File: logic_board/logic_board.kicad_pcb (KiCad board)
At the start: 4 copper layers, 80 x 30 mm, 55 parts, among them J1 Debug, J2 Audio In, J3 SJ2-3595X-SMT, J4 Amphenol 124015, J5 Batt, SW1 TL3315NF160Q, SW2 TL3315NF160Q, SW3 TL3315NF160Q, SW4 TL3315NF160Q, SW5 Power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

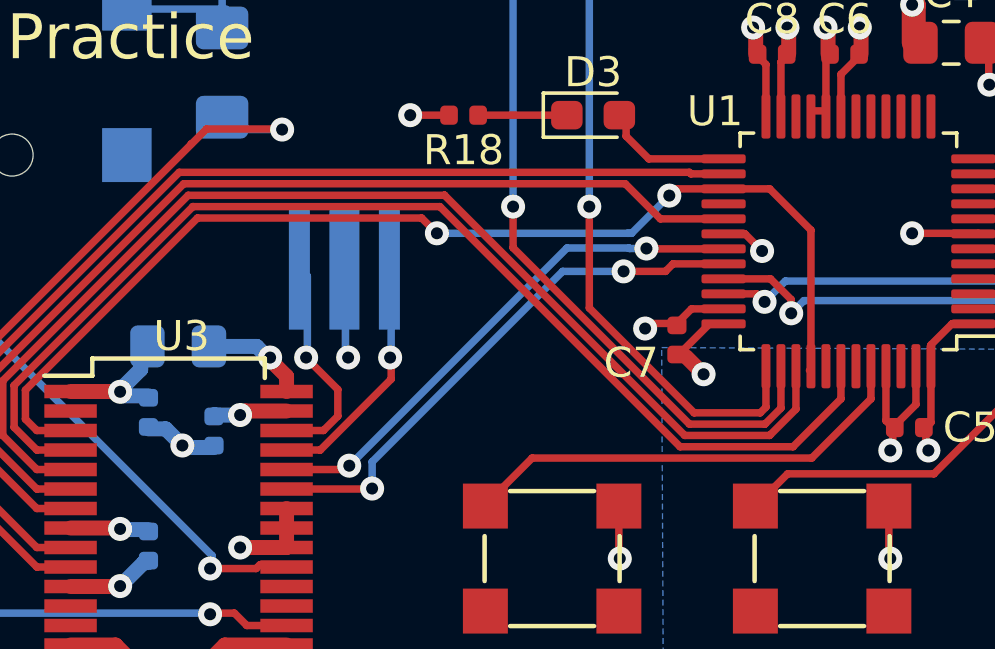
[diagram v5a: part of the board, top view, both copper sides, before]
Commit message: Fix I2C2_SDA, which was mislabeled in the STM32G473 datasheet.
It now connects to pin30. In the G474 datasheet, both places
that reference this pin agree.
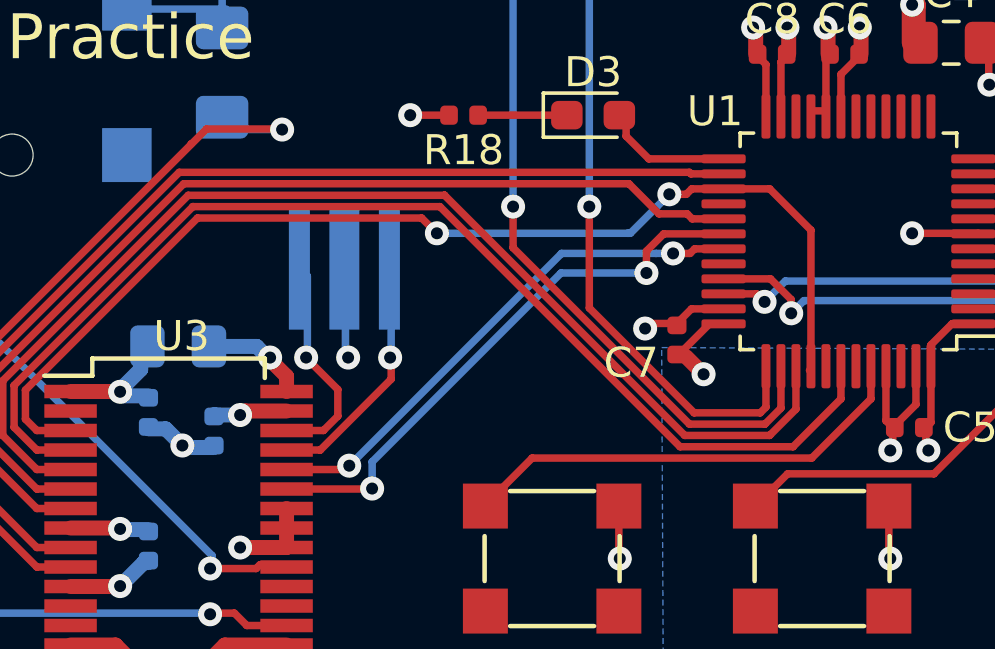
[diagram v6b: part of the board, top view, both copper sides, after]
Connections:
- U1 pad 30: Net-(U1-Pad30) -> SDA
- U1 pad 32: SDA -> Net-(U1-Pad32)
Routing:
- net Net-(U1-Pad30): track 1.77 -> 0.00 mm, vias 1 -> 0
- net SDA: track 18.0 -> 19.0 mm
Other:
- net class Default: trace_width 0.127 -> 0.25

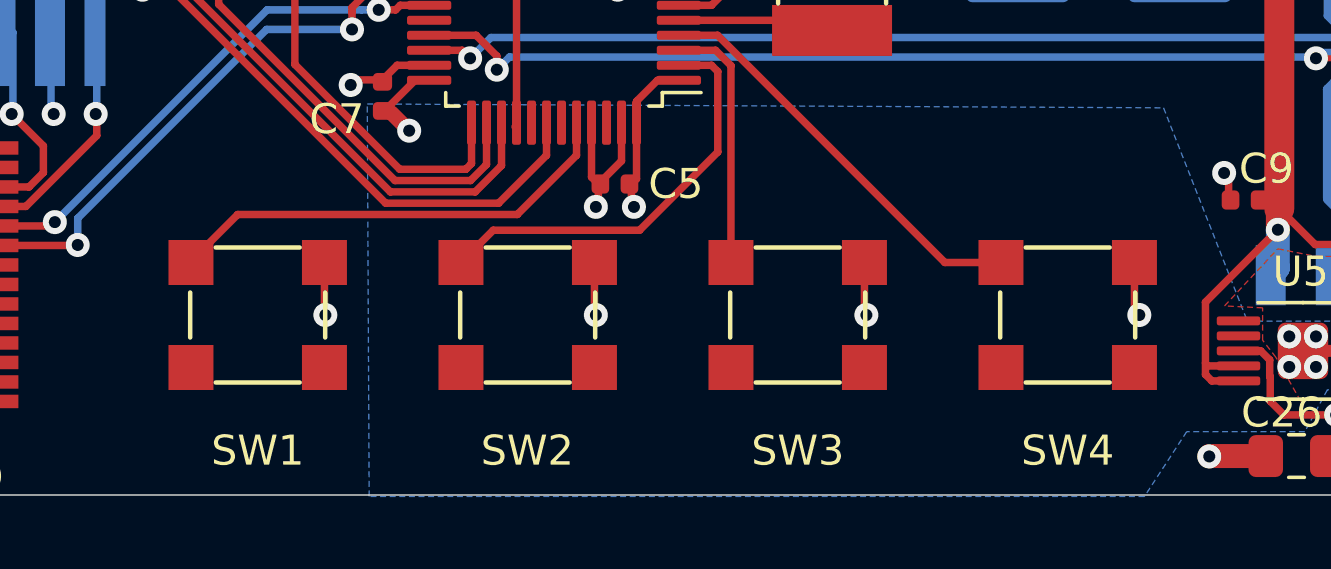
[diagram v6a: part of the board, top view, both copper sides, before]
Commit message: The custom footprint for the tactile had the pins misnumbered
They were rotated 90 degrees. There are actually four pins, with
two on each side connected internally. There doesn't seem to be
an easy way to indicate that in kicad, so only two are connected
to the schematic symbol.
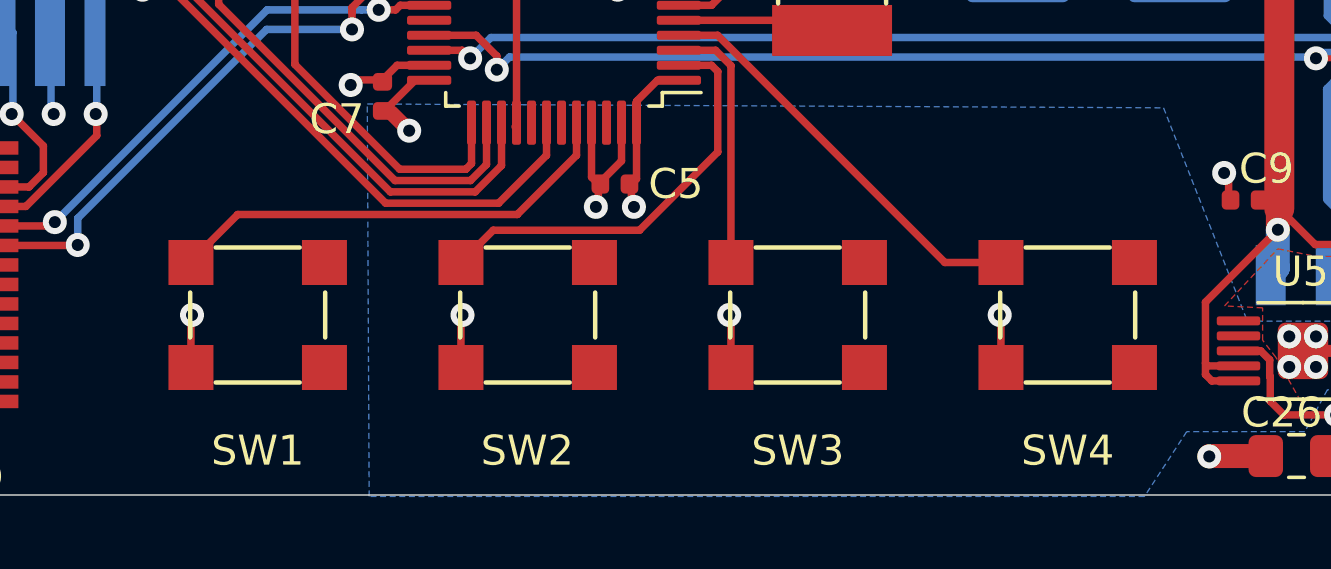
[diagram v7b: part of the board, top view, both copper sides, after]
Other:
- net class Default: via_dia 0.4572 -> 0.8; via_drill 0.254 -> 0.4
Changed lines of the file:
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@@
     (zone_45_only no)
     (trace_min 0.127)
-    (via_size 0.4572)
-    (via_drill 0.254)
+    (via_size 0.8)
+    (via_drill 0.4)
     (via_min_size 0.4572)
     (via_min_drill 0.254)
@@
     (clearance 0.127)
     (trace_width 0.25)
-    (via_dia 0.4572)
-    (via_drill 0.254)
+    (via_dia 0.8)
+    (via_drill 0.4)
     (uvia_dia 0.4572)
     (uvia_drill 0.254)
@@
     (fp_line (start -3.3 -3) (end 3.3 -3) (layer F.CrtYd) (width 0.12))
     (pad 4 smd rect (at 2.225 1.75) (size 1.5 1.5) (layers F.Cu F.Paste F.Mask))
-    (pad 3 smd rect (at -2.225 1.75) (size 1.5 1.5) (layers F.Cu F.Paste F.Mask))
-    (pad 2 smd rect (at 2.225 -1.75) (size 1.5 1.5) (layers F.Cu F.Paste F.Mask)
-      (net 2 GND))
+    (pad 2 smd rect (at -2.225 1.75) (size 1.5 1.5) (layers F.Cu F.Paste F.Mask)
+      (net 2 GND))
+    (pad 3 smd rect (at 2.225 -1.75) (size 1.5 1.5) (layers F.Cu F.Paste F.Mask))
     (pad 1 smd rect (at -2.225 -1.75) (size 1.5 1.5) (layers F.Cu F.Paste F.Mask)
       (net 60 SW4))
@@
     (fp_line (start -3.3 -3) (end 3.3 -3) (layer F.CrtYd) (width 0.12))
     (pad 4 smd rect (at 2.225 1.75) (size 1.5 1.5) (layers F.Cu F.Paste F.Mask))
-    (pad 3 smd rect (at -2.225 1.75) (size 1.5 1.5) (layers F.Cu F.Paste F.Mask))
-    (pad 2 smd rect (at 2.225 -1.75) (size 1.5 1.5) (layers F.Cu F.Paste F.Mask)
-      (net 2 GND))
+    (pad 2 smd rect (at -2.225 1.75) (size 1.5 1.5) (layers F.Cu F.Paste F.Mask)
+      (net 2 GND))
+    (pad 3 smd rect (at 2.225 -1.75) (size 1.5 1.5) (layers F.Cu F.Paste F.Mask))
     (pad 1 smd rect (at -2.225 -1.75) (size 1.5 1.5) (layers F.Cu F.Paste F.Mask)
       (net 59 SW3))
@@
     (fp_line (start -3.3 -3) (end 3.3 -3) (layer F.CrtYd) (width 0.12))
     (pad 4 smd rect (at 2.225 1.75) (size 1.5 1.5) (layers F.Cu F.Paste F.Mask))
-    (pad 3 smd rect (at -2.225 1.75) (size 1.5 1.5) (layers F.Cu F.Paste F.Mask))
-    (pad 2 smd rect (at 2.225 -1.75) (size 1.5 1.5) (layers F.Cu F.Paste F.Mask)
-      (net 2 GND))
+    (pad 2 smd rect (at -2.225 1.75) (size 1.5 1.5) (layers F.Cu F.Paste F.Mask)
+      (net 2 GND))
+    (pad 3 smd rect (at 2.225 -1.75) (size 1.5 1.5) (layers F.Cu F.Paste F.Mask))
     (pad 1 smd rect (at -2.225 -1.75) (size 1.5 1.5) (layers F.Cu F.Paste F.Mask)
       (net 58 SW2))
@@
     (fp_line (start -3.3 -3) (end 3.3 -3) (layer F.CrtYd) (width 0.12))
     (pad 4 smd rect (at 2.225 1.75) (size 1.5 1.5) (layers F.Cu F.Paste F.Mask))
-    (pad 3 smd rect (at -2.225 1.75) (size 1.5 1.5) (layers F.Cu F.Paste F.Mask))
-    (pad 2 smd rect (at 2.225 -1.75) (size 1.5 1.5) (layers F.Cu F.Paste F.Mask)
-      (net 2 GND))
+    (pad 2 smd rect (at -2.225 1.75) (size 1.5 1.5) (layers F.Cu F.Paste F.Mask)
+      (net 2 GND))
+    (pad 3 smd rect (at 2.225 -1.75) (size 1.5 1.5) (layers F.Cu F.Paste F.Mask))
     (pad 1 smd rect (at -2.225 -1.75) (size 1.5 1.5) (layers F.Cu F.Paste F.Mask)
       (net 57 SW1))
@@
   (via (at 167.386 124.714) (size 0.8) (drill 0.4) (layers F.Cu B.Cu) (net 2) (status 30))
   (via (at 155.067 112.014) (size 0.8) (drill 0.4) (layers F.Cu B.Cu) (net 2))
-  (via (at 162.38728 124) (size 0.8) (drill 0.4) (layers F.Cu B.Cu) (net 2))
-  (via (at 153.289 124) (size 0.8) (drill 0.4) (layers F.Cu B.Cu) (net 2))
-  (via (at 144.272 124) (size 0.8) (drill 0.4) (layers F.Cu B.Cu) (net 2))
-  (via (at 135.255 124) (size 0.8) (drill 0.4) (layers F.Cu B.Cu) (net 2))
   (via (at 126.2 117.3) (size 0.8) (drill 0.4) (layers F.Cu B.Cu) (net 2))
   (via (at 169.926 122.682) (size 0.8) (drill 0.4) (layers F.Cu B.Cu) (net 2))
@@
   (segment (start 170.376 110.156) (end 171.09 110.87) (width 0.25) (layer B.Cu) (net 2) (status 20))
   (segment (start 170.376 107.95) (end 170.376 110.156) (width 0.25) (layer B.Cu) (net 2) (status 10))
-  (segment (start 135.225 124.049) (end 135.255 124.079) (width 0.25) (layer F.Cu) (net 2))
-  (segment (start 135.225 122.25) (end 135.225 124.049) (width 0.25) (layer F.Cu) (net 2) (status 10))
-  (segment (start 144.225 123.905) (end 144.272 123.952) (width 0.25) (layer F.Cu) (net 2))
-  (segment (start 144.225 122.25) (end 144.225 123.905) (width 0.25) (layer F.Cu) (net 2) (status 10))
-  (segment (start 153.225 123.888) (end 153.289 123.952) (width 0.25) (layer F.Cu) (net 2))
-  (segment (start 153.225 122.25) (end 153.225 123.888) (width 0.25) (layer F.Cu) (net 2) (status 10))
-  (segment (start 162.225 123.91672) (end 162.38728 124.079) (width 0.25) (layer F.Cu) (net 2))
-  (segment (start 162.225 122.25) (end 162.225 123.91672) (width 0.25) (layer F.Cu) (net 2) (status 10))
   (segment (start 152.146 112.014) (end 155.067 112.014) (width 0.25) (layer F.Cu) (net 2) (status 10))
   (segment (start 164.7317 128.7018) (end 164.719 128.7145) (width 0.8) (layer F.Cu) (net 2))
@@
   (segment (start 168.6832 125.1966) (end 169.9932 125.1966) (width 0.4) (layer F.Cu) (net 2) (status 20))
   (segment (start 167.8432 125.1966) (end 168.6832 125.1966) (width 0.127) (layer F.Cu) (net 2) (status 10))
+  (via (at 139.827 124) (size 0.8) (drill 0.4) (layers F.Cu B.Cu) (net 2))
+  (segment (start 139.775 124.131) (end 139.827 124.079) (width 0.25) (layer F.Cu) (net 2))
+  (segment (start 139.775 125.75) (end 139.775 124.131) (width 0.25) (layer F.Cu) (net 2))
+  (via (at 148.717 124) (size 0.8) (drill 0.4) (layers F.Cu B.Cu) (net 2))
+  (segment (start 148.775 124.01) (end 148.717 123.952) (width 0.25) (layer F.Cu) (net 2))
+  (segment (start 148.775 125.75) (end 148.775 124.01) (width 0.25) (layer F.Cu) (net 2))
+  (segment (start 157.775 124.12) (end 157.734 124.079) (width 0.25) (layer F.Cu) (net 2))
+  (via (at 157.734 124) (size 0.8) (drill 0.4) (layers F.Cu B.Cu) (net 2))
+  (segment (start 157.775 125.75) (end 157.775 124.12) (width 0.25) (layer F.Cu) (net 2))
+  (via (at 130.81 124) (size 0.8) (drill 0.4) (layers F.Cu B.Cu) (net 2))
+  (segment (start 130.775 124.114) (end 130.81 124.079) (width 0.25) (layer F.Cu) (net 2))
+  (segment (start 130.775 125.75) (end 130.775 124.114) (width 0.25) (layer F.Cu) (net 2))
   (segment (start 166.4628 120.1674) (end 166.7637 120.1674) (width 0.4) (layer F.Cu) (net 3) (status 10))
   (via (at 167.005 121.158) (size 0.8) (drill 0.4) (layers F.Cu B.Cu) (net 3))
@@
     (polygon
       (pts
-        (xy 163.068 124.841) (xy 161.4805 124.841) (xy 161.4805 123.19) (xy 163.068 123.19)
+        (xy 158.623 124.841) (xy 157.0355 124.841) (xy 157.0355 123.19) (xy 158.623 123.19)
       )
     )
@@
     (polygon
       (pts
-        (xy 154.051 124.841) (xy 152.4 124.841) (xy 152.4 123.19) (xy 154.051 123.19)
+        (xy 149.606 124.841) (xy 147.955 124.841) (xy 147.955 123.19) (xy 149.606 123.19)
       )
     )
@@
     (polygon
       (pts
-        (xy 145.034 124.841) (xy 143.383 124.841) (xy 143.383 123.19) (xy 145.034 123.19)
+        (xy 140.589 124.841) (xy 138.938 124.841) (xy 138.938 123.19) (xy 140.589 123.19)
       )
     )

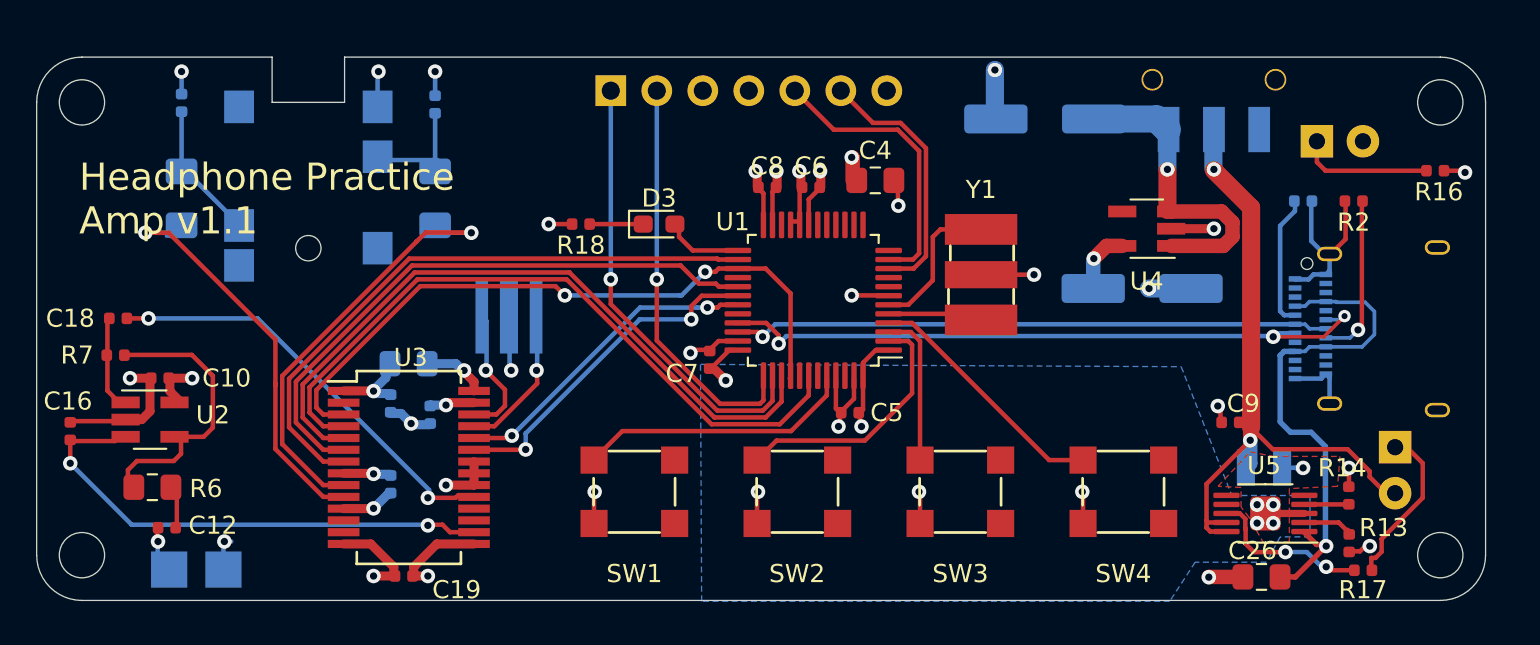
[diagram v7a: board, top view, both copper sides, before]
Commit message: Use through-hole USB C connector for easier soldering.
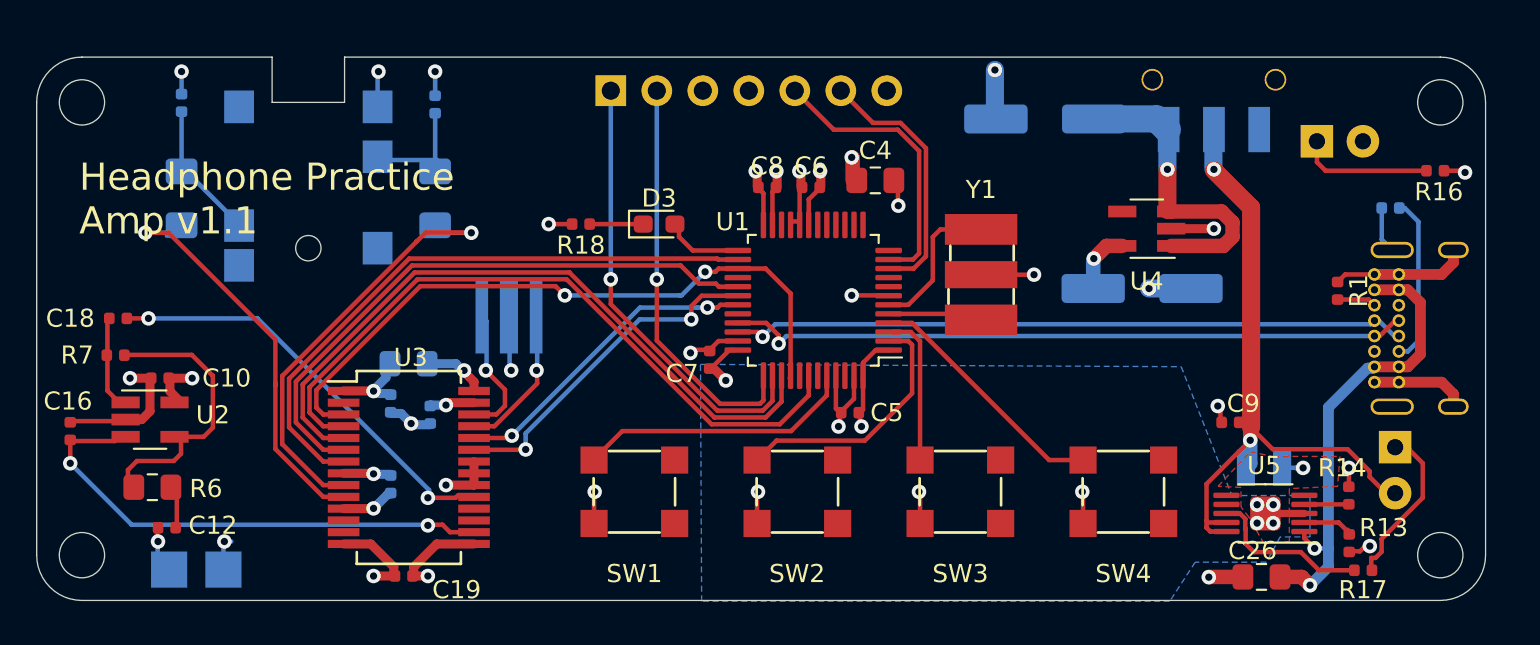
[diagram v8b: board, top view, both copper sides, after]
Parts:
- J4: footprint Connector_USB:USB_C_Receptacle_Amphenol_12401610E4-2A -> Connector_USB:USB_C_Receptacle_GCT_USB4085
- R1: moved to F.Cu
- R2: moved to B.Cu
- moved R1 5.31 mm to (171.8, 112.9), turned to 270 degrees
- moved J4 3.07 mm to (173.9, 112.0)
- moved R2 2.07 mm to (174.8, 108.3)
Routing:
- net Net-(J4-PadA5): track 7.33 -> 2.16 mm
- net USB_DP: track 33.5 -> 37.9 mm
- net Net-(C26-Pad1): track 28.5 -> 26.0 mm, vias 1 -> 2
- net GND: track 90.5 -> 92.3 mm
- net USB_DM: track 37.5 -> 38.0 mm, vias 3 -> 1
- net Net-(J4-PadB5): track 9.16 -> 9.27 mm, vias 1 -> 0
- net Net-(R17-Pad2): track 9.13 -> 9.15 mm, vias 2 -> 0
